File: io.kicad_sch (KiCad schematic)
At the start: 17 parts, among them J1 Conn_02x04_Odd_Even, J2 Conn_02x04_Odd_Even, J3 Conn_02x04_Odd_Even, J4 Conn_02x04_Odd_Even, J5 Conn_02x04_Odd_Even, J6 Conn_02x04_Odd_Even, J7 Conn_02x04_Odd_Even, J8 Conn_02x04_Odd_Even, J9 Conn_01x03

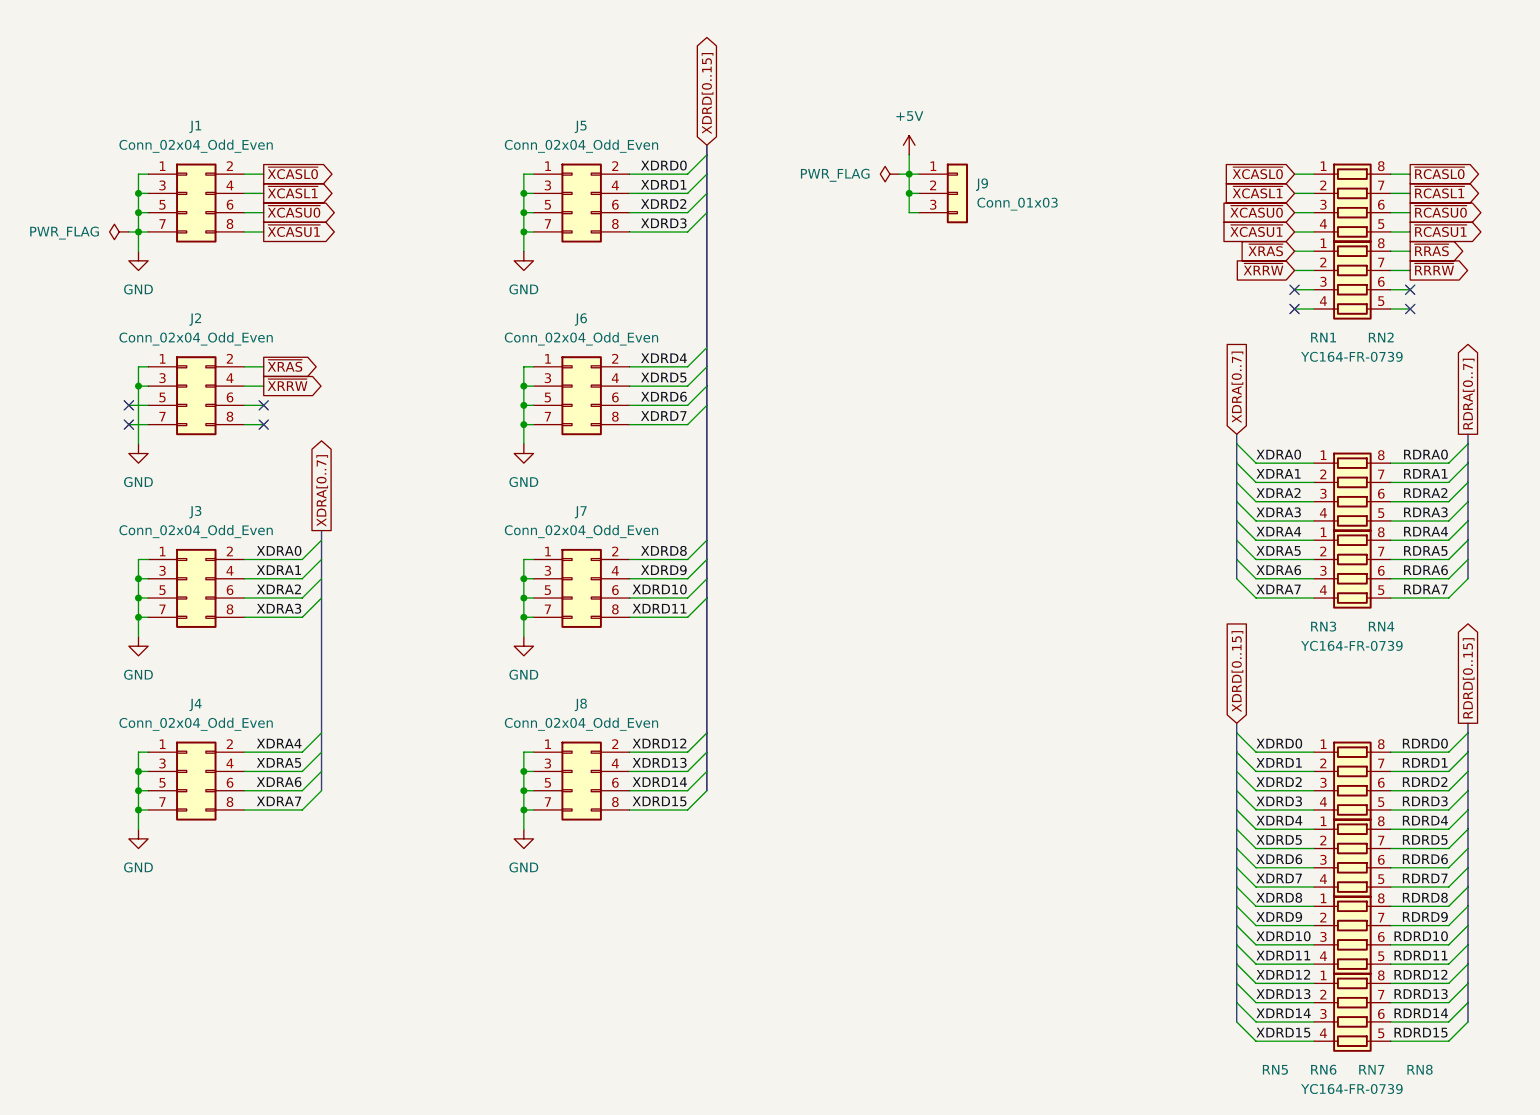
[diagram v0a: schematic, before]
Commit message: Update Schematic for card edge connector
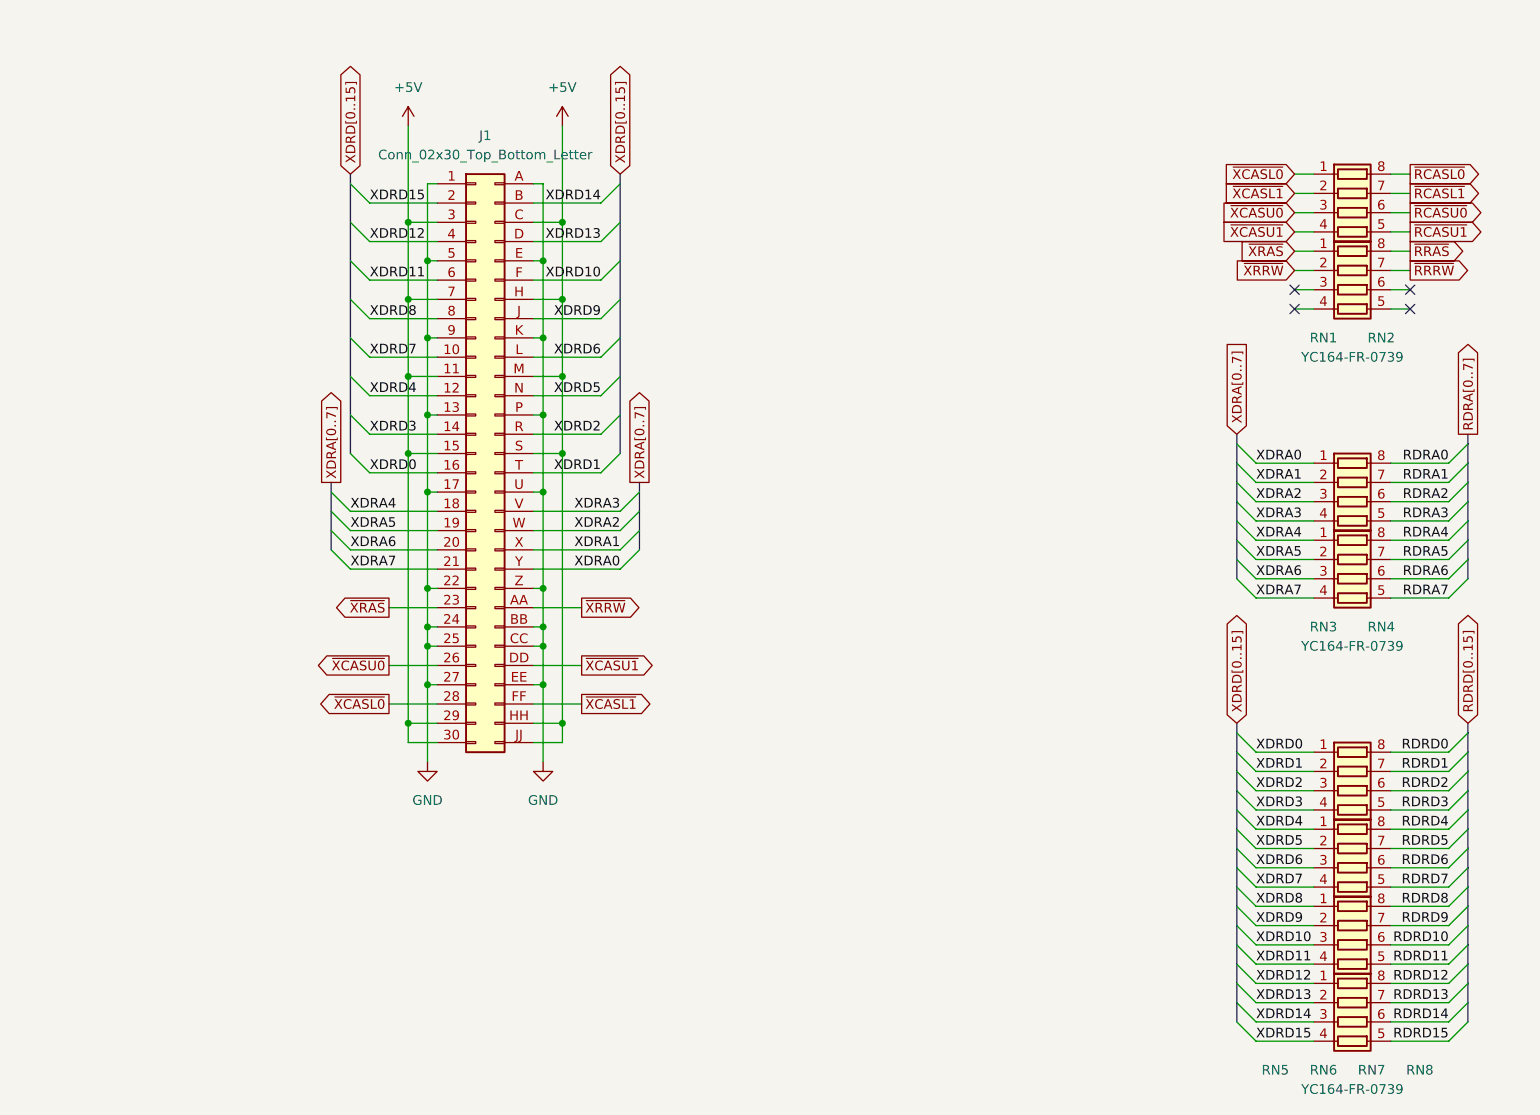
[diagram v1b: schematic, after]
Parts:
- removed J1, J2, J3, J4, J5, J6, J7, J8: Conn_02x04_Odd_Even, Connector_PinHeader_2.54mm:PinHeader_2x04_P2.54mm_Vertical, symbol Connector_Generic:Conn_02x04_Odd_Even
- removed J9: Conn_01x03, Connector_PinHeader_2.54mm:PinHeader_1x03_P2.54mm_Vertical, symbol Connector_Generic:Conn_01x03
- added J1: Conn_02x30_Top_Bottom_Letter, AmigaA1000RAM:CardEdgeSocket_2x30_P3.96mm, symbol AmigaA1000RAM:Conn_02x30_Top_Bottom_Letter
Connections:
- net +5V: now also J1.11 (Pin_11), J1.15 (Pin_15), J1.29 (Pin_29), J1.3 (Pin_3), J1.30 (Pin_30), J1.7 (Pin_7), J1.C (Pin_C), J1.H (Pin_H), J1.HH (Pin_HH), J1.JJ (Pin_JJ), J1.M (Pin_M), J1.S (Pin_S)
- net GND: now also J1.1 (Pin_1), J1.13 (Pin_13), J1.17 (Pin_17), J1.22 (Pin_22), J1.24 (Pin_24), J1.25 (Pin_25), J1.27 (Pin_27), J1.5 (Pin_5), J1.9 (Pin_9), J1.A (Pin_A), J1.BB (Pin_BB), J1.CC (Pin_CC), J1.E (Pin_E), J1.EE (Pin_EE), J1.K (Pin_K), J1.P (Pin_P), J1.U (Pin_U), J1.Z (Pin_Z)
- net XDRA0: now also J1.Y (Pin_Y)
- net XDRA1: now also J1.X (Pin_X)
- net XDRA2: now also J1.W (Pin_W)
- net XDRA3: now also J1.V (Pin_V)
- net XDRA4: now also J1.18 (Pin_18)
- net XDRA5: now also J1.19 (Pin_19)
- net XDRA6: now also J1.20 (Pin_20)
- net XDRA7: now also J1.21 (Pin_21)
- net XDRD0: now also J1.16 (Pin_16)
- net XDRD1: now also J1.T (Pin_T)
- net XDRD10: now also J1.F (Pin_F)
- net XDRD11: now also J1.6 (Pin_6)
- net XDRD12: now also J1.4 (Pin_4)
- net XDRD13: now also J1.D (Pin_D)
- net XDRD14: now also J1.B (Pin_B)
- net XDRD15: now also J1.2 (Pin_2)
- net XDRD2: now also J1.R (Pin_R)
- net XDRD3: now also J1.14 (Pin_14)
- net XDRD4: now also J1.12 (Pin_12)
- net XDRD5: now also J1.N (Pin_N)
- net XDRD6: now also J1.L (Pin_L)
- net XDRD7: now also J1.10 (Pin_10)
- net XDRD8: now also J1.8 (Pin_8)
- net XDRD9: now also J1.J (Pin_J)
- net ~{XCASL0}: now also J1.28 (Pin_28)
- net ~{XCASL1}: now also J1.FF (Pin_FF)
- net ~{XCASU0}: now also J1.26 (Pin_26)
- net ~{XCASU1}: now also J1.DD (Pin_DD)
- net ~{XRAS}: now also J1.23 (Pin_23)
- net ~{XRRW}: now also J1.AA (Pin_AA)
- no-connect marks 8 -> 4
